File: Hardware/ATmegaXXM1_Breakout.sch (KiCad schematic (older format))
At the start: 11 parts

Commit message: Finished rev 1.0 schematic & BOM
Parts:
- added C4, C5: 4.7uF, Capacitors_SMD:C_0805, symbol C
- added C8: 100nF, Capacitors_SMD:C_0805, symbol C
- added D1: POWER_LED, LEDs:LED_0805, symbol LED
- added P1: VIN, FritzLib:2x01_ScrewTerm, symbol CONN_01X02
- added P10: UART, Pin_Headers:Pin_Header_Straight_1x03, symbol CONN_01X03
- added P2: PORTB, Pin_Headers:Pin_Header_Straight_1x08, symbol CONN_01X08
- added P3: PORTC, Pin_Headers:Pin_Header_Straight_1x07, symbol CONN_01X07
- added P4: PORTD, Pin_Headers:Pin_Header_Straight_1x08, symbol CONN_01X08
- added P5: PD3, Pin_Headers:Pin_Header_Straight_2x02, symbol CONN_02X02
- added P6: PD4, Pin_Headers:Pin_Header_Straight_2x02, symbol CONN_02X02
- added P7: CAN_R, Pin_Headers:Pin_Header_Straight_1x02, symbol CONN_01X02
- added P9: CAN, FritzLib:2x01_ScrewTerm, symbol CONN_01X02
- added R1, R3: 470, Resistors_SMD:R_0805, symbol R
- added R4: 10k, Resistors_SMD:R_0805, symbol R
- added R5: 120, Resistors_SMD:R_1206, symbol R
- added U2: MIC5235, TO_SOT_Packages_SMD:SOT-23-5, symbol MIC5235
- added U3: ATA6560, Housings_SOIC:SOIC-8_3.9x4.9mm_Pitch1.27mm, symbol ATA6560
- C1, C2, C3, C6, C7: renamed from C?; footprint (none) -> Capacitors_SMD:C_0805
- D2: renamed from D?; footprint (none) -> LEDs:LED_0805
- P8: renamed from P?; footprint (none) -> Pin_Headers:Pin_Header_Straight_2x03
- R2: renamed from R?; footprint (none) -> Resistors_SMD:R_0805
- SW1: renamed from SW?; footprint (none) -> Buttons_Switches_SMD:SW_SPST_EVQPE1
- U1: renamed from IC?; footprint TQFP32 -> Housings_QFP:TQFP-32_7x7mm_Pitch0.8mm
- Y1: renamed from Y?; footprint (none) -> Crystals:Crystal_HC49-SD_SMD
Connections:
- net +5V: now also D2.2 (A), C5.1, C8.1, D1.2 (A), R4.1, U2.5 (OUT), U3.3 (VCC), U3.5 (NSIL); no longer C3.1, U1.21 (AREF(ISRC))
- net AVR_MISO: now also U1.1 ((PCINT18/PSCIN2/OC1A/MISO_A)PD2), P4.3 (P3)
- net AVR_MOSI: now also P5.4 (P4)
- net AVR_SCK: now also P6.4 (P4); no longer U1.28 ((PCINT7/ADC4/SCK/PSCOUT0B)PB7)
- net GND: now also C4.2, C5.2, C8.2, P1.2 (P2), P10.3 (P3), R1.1, U2.2 (GND), U3.2 (GND), U3.8 (STBY)
- net PD4: now reaches U1.12 ((PCINT20/ADC1/RXD/RXLIN/ICP1A/SCK_A)PD4)
- net PD4: now also P4.5 (P5), P6.1 (P1), P6.3 (P3)
- net PD5: now reaches U1.13 ((PCINT21/ADC2/ACMP2)PD5)
- net PD5: now also P4.6 (P6)
- net PD6: now reaches U1.14 ((PCINT22/ADC3/INT0/ACMPN2)PD6)
- net PD6: now also P4.7 (P7)
- net PD7: now reaches U1.15 ((PCINT23/ACMP0)PD7)
- net PD7: now also P4.8 (P8)
- net PB2: now reaches U1.16 ((PCINT2/ADC5/INT1/ACMPN0)PB2)
- net PB2: now also P2.3 (P3)
- net PC4: now reaches U1.17 ((PCINT12/ADC8/ACMPN3/AMP1-)PC4)
- net PC4: now also P3.3 (P3)
- net PC5: now reaches U1.18 ((PCINT13/ADC9/ACMP3/AMP1+)PC5)
- net PC5: now also P3.4 (P4)
- net PD3: now reaches U1.2 ((PCINT19/TXD/TXLIN/OC0A/~SS~/MOSI_A)PD3)
- net PD3: now also P4.4 (P4), P5.1 (P1), P5.3 (P3)
- net PC6: now reaches U1.22 ((PCINT14/ADC10/ACMP1)PC6)
- net PC6: now also P3.5 (P5)
- net PB3: now reaches U1.23 ((PCINT3/AMP0-)PB3)
- net PB3: now also P2.4 (P4)
- net PB4: now reaches U1.24 ((PCINT4/AMP0+)PB4)
- net PB4: now also P2.5 (P5)
- net PC7: now reaches U1.25 ((PCINT15/D2A/AMP2+)PC7)
- net PC7: now also P3.6 (P6), R3.1
- net PB5: now reaches U1.26 ((PCINT5/ADC6/INT2/ACMPN1/AMP2-)PB5)
- net PB5: now also P2.6 (P6)
- net PB6: now reaches U1.27 ((PCINT6/ADC7/PSCOUT1B)PB6)
- net PB6: now also P2.7 (P7)
- net PD0: now reaches U1.29 ((PCINT16/PSCOUT0A)PD0)
- net PD0: now also P4.1 (P1)
- net PC1: now reaches U1.3 ((PCINT9/PSCIN1/OC1B/~SS_A~)PC1)
- net PC1: now also P3.2 (P2)
- net PC0: now reaches U1.30 ((PCINT8/INT3/PSCOUT1A)PC0)
- net PC0: now also P3.1 (P1)
- net PD1: now reaches U1.32 ((PCINT17/CLKO/PSCIN0)PD1)
- net PD1: now also P4.2 (P2)
- net TXCAN: now reaches U1.6 ((PCINT10/T0/TXCAN)PC2)
- net TXCAN: now also R4.2, U3.1 (D)
- net RXCAN: now reaches U1.7 ((PCINT11/T1/ICP1B/RXCAN)PC3)
- net RXCAN: now also U3.4 (R)
- net PB0: now reaches U1.8 ((PCINT0/MISO/PSCOUT2A)PB0)
- net PB0: now also P2.1 (P1)
- net PB1: now reaches U1.9 ((PCINT1/MOSI/PSCOUT2B)PB1)
- net PB1: now also P2.2 (P2)
- net at D2.1 (K): now also R3.2
- new net: D1.1 (K), R1.2
- new net: P7.1 (P1), R5.1
- new net AREF: C3.1, P3.7 (P7), U1.21 (AREF(ISRC))
- new net AVR_RX: P10.2 (P2), P6.2 (P2)
- new net AVR_TX: P10.1 (P1), P5.2 (P2)
- new net CAN+: P9.1 (P1), R5.2, U3.7 (CANH)
- new net CAN-: P7.2 (P2), P9.2 (P2), U3.6 (CANL)
- new net PB7: P2.8 (P8), U1.28 ((PCINT7/ADC4/SCK/PSCOUT0B)PB7)
- new net VIN: C4.1, P1.1 (P1), U2.1 (IN), U2.3 (EN)
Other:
- note added: "NOTE: In order to program the AVR\nPD3 & PD4 MUST be set to their \nrespective SPI functions"
- note added: "Select function of PD3 pin:\nUART Tx and/or SPI MOSI"
- note added: "Select function of PD4 pin:\nUART Rx and/or SPI SCK"
- moved on the sheet: C1, C2, C3, C6, C7, D2, P8, R2, SW1, U1, Y1

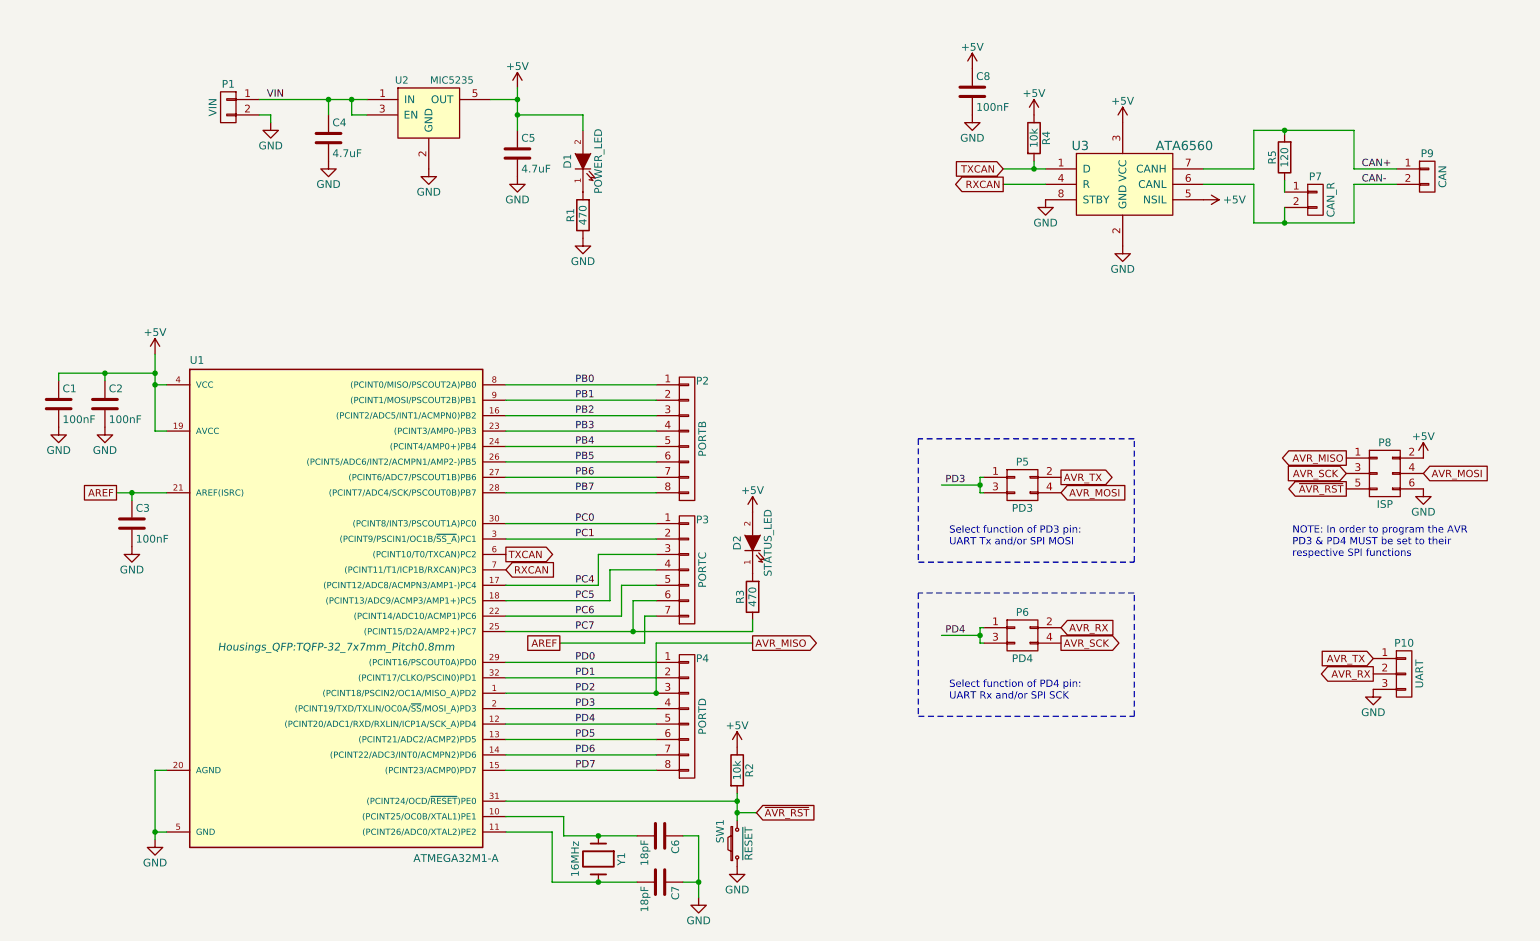
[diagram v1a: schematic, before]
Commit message: Finished routing & added mouting holes
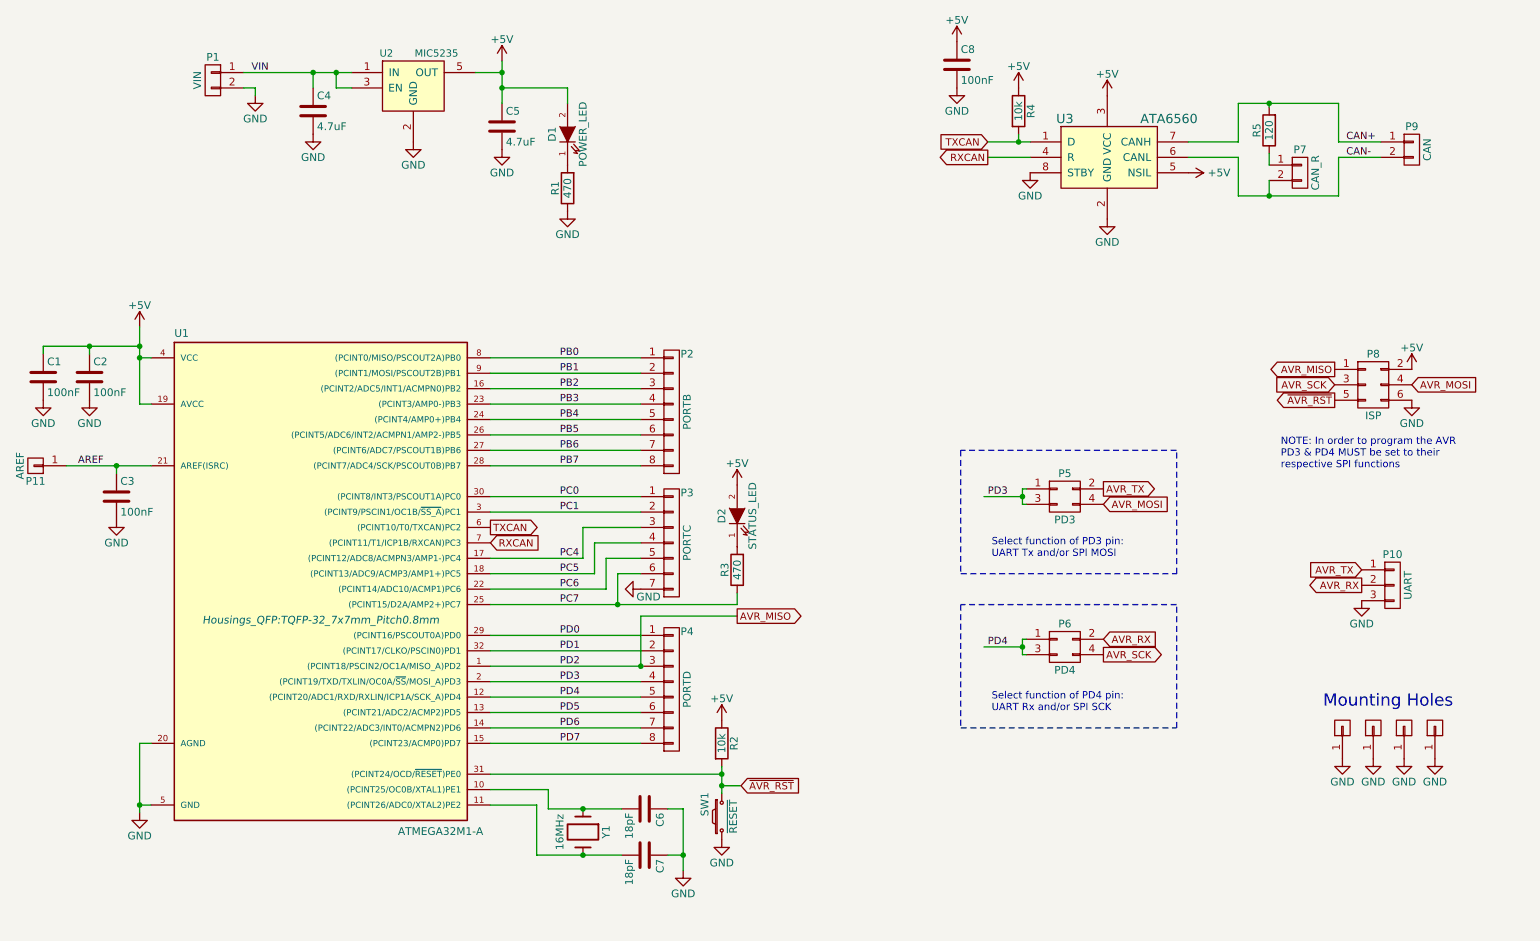
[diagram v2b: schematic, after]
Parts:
- added P11: AREF, Pin_Headers:Pin_Header_Straight_1x01, symbol CONN_01X01
- added P? (x4): Mounting Hole, symbol CONN_01X01
- R1, R2, R3, R4: footprint Resistors_SMD:R_0805 -> Capacitors_SMD:C_0805
- R5: footprint Resistors_SMD:R_1206 -> Capacitors_SMD:C_1206
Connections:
- net AREF: now also P11.1 (P1); no longer P3.7 (P7)
- net GND: now also P3.7 (P7), P?.1 (P1), P?.1 (P1), P?.1 (P1), P?.1 (P1)
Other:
- note added: "Mounting Holes"
- moved on the sheet: C1, C2, C3, C4, C5, C6, C7, C8, D1, D2, P1, P10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
